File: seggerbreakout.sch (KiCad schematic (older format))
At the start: 3 parts, among them P1 SWD, P2 JTAG

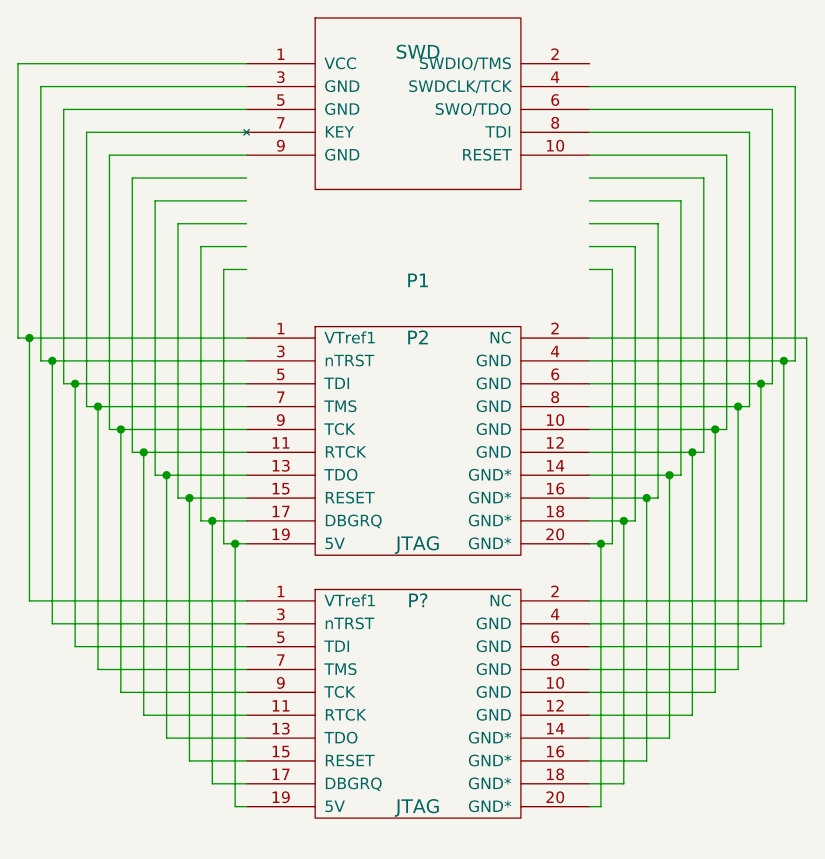
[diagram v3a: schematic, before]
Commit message: add swd and 2x5 swd connector
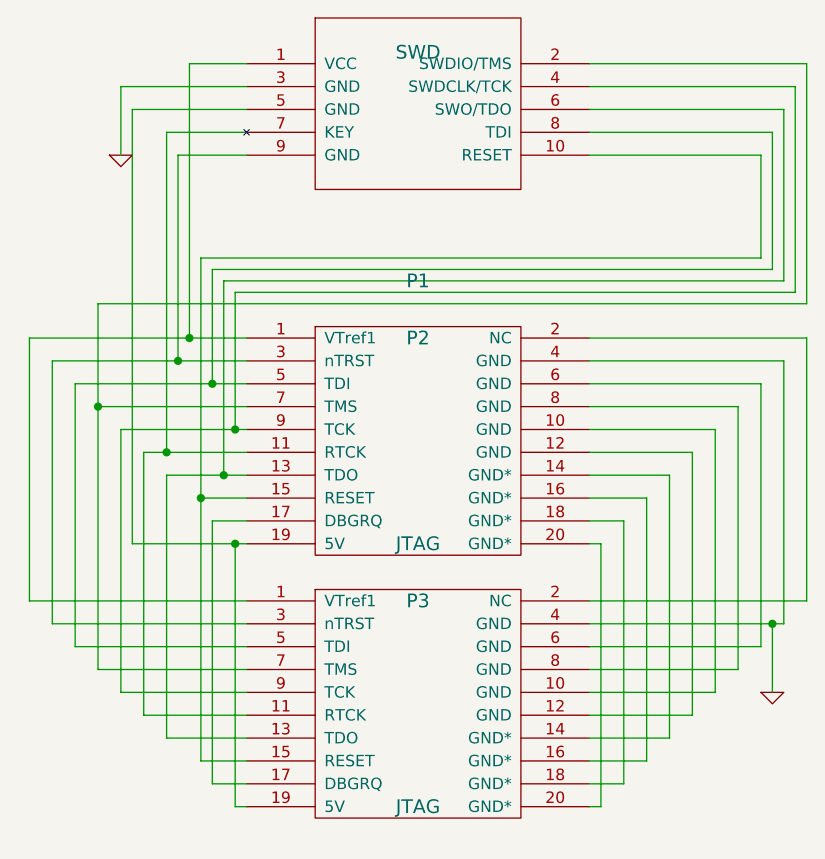
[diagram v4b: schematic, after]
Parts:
- gave numbers to parts that had none: 1
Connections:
- net labels added: GND
- wire segments 98 -> 89
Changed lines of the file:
@@
 Sheet 1 1
 Title ""
-Date "18 apr 2014"
+Date "18 aug 2014"
 Rev ""
 Comp ""
@@
 $EndComp
 $Comp
-L JTAG P?
+L JTAG P3
 U 1 1 53516C39
 P 5150 5700
-F 0 "P?" H 5150 6150 60  0000 C CNN
+F 0 "P3" H 5150 6150 60  0000 C CNN
 F 1 "JTAG" H 5150 5250 60  0000 C CNN
 F 2 "~" H 5050 5750 60  0000 C CNN
@@
 $EndComp
 Wire Wire Line
-	4300 5000 4400 5000
-Wire Wire Line
-	4300 5000 4300 3800
-Wire Wire Line
-	4300 3800 4400 3800
-Wire Wire Line
-	4400 3700 4200 3700
-Wire Wire Line
-	4200 3700 4200 4900
-Wire Wire Line
-	4200 4900 4400 4900
-Wire Wire Line
-	4400 3600 4100 3600
-Wire Wire Line
-	4100 3600 4100 4800
-Wire Wire Line
-	4100 4800 4400 4800
-Wire Wire Line
-	4400 3500 4000 3500
-Wire Wire Line
-	4000 3500 4000 4700
-Wire Wire Line
-	4000 4700 4400 4700
-Wire Wire Line
-	4400 3300 3800 3300
-Wire Wire Line
-	3800 3300 3800 4500
-Wire Wire Line
-	3800 4500 4400 4500
-Wire Wire Line
-	4400 3200 3700 3200
-Wire Wire Line
-	3700 3200 3700 4400
-Wire Wire Line
-	3700 4400 4400 4400
-Wire Wire Line
-	4400 3100 3600 3100
-Wire Wire Line
-	3600 3100 3600 4300
-Wire Wire Line
-	3600 4300 4400 4300
-Wire Wire Line
-	4400 3000 3500 3000
-Wire Wire Line
-	3500 3000 3500 4200
-Wire Wire Line
-	3500 4200 4400 4200
-Wire Wire Line
-	4400 2900 3400 2900
-Wire Wire Line
-	3400 2900 3400 4100
-Wire Wire Line
-	3400 4100 4400 4100
-Wire Wire Line
-	5900 3800 6000 3800
-Wire Wire Line
-	6000 3800 6000 5000
-Wire Wire Line
-	6000 5000 5900 5000
-Wire Wire Line
-	5900 4900 6100 4900
-Wire Wire Line
-	6100 4900 6100 3700
-Wire Wire Line
-	6100 3700 5900 3700
-Wire Wire Line
-	5900 4800 6200 4800
-Wire Wire Line
-	6200 4800 6200 3600
-Wire Wire Line
-	6200 3600 5900 3600
-Wire Wire Line
-	5900 4700 6300 4700
-Wire Wire Line
-	6300 4700 6300 3500
-Wire Wire Line
-	6300 3500 5900 3500
-Wire Wire Line
-	5900 4600 6400 4600
-Wire Wire Line
-	6400 4600 6400 3400
-Wire Wire Line
-	6400 3400 5900 3400
-Wire Wire Line
-	5900 4500 6500 4500
-Wire Wire Line
-	6500 4500 6500 3300
-Wire Wire Line
-	6500 3300 5900 3300
-Wire Wire Line
-	5900 4400 6600 4400
-Wire Wire Line
-	6600 4400 6600 3200
-Wire Wire Line
-	6600 3200 5900 3200
-Wire Wire Line
-	5900 4300 6700 4300
-Wire Wire Line
-	6700 4300 6700 3100
-Wire Wire Line
-	6700 3100 5900 3100
-Wire Wire Line
-	5900 4200 6800 4200
-Wire Wire Line
-	6800 4200 6800 3000
+	4350 5000 4350 6150
+Wire Wire Line
+	4350 6150 4400 6150
+Wire Wire Line
+	4250 4900 4250 6050
+Wire Wire Line
+	4250 6050 4400 6050
+Wire Wire Line
+	4050 4700 4050 5850
+Wire Wire Line
+	4050 5850 4400 5850
+Wire Wire Line
+	3950 4600 3950 5750
+Wire Wire Line
+	3950 5750 4400 5750
+Wire Wire Line
+	3850 4500 3850 5650
+Wire Wire Line
+	3850 5650 4400 5650
+Wire Wire Line
+	3750 3950 3750 5550
+Wire Wire Line
+	3750 5550 4400 5550
+Wire Wire Line
+	3650 4300 3650 5450
+Wire Wire Line
+	3650 5450 4400 5450
+Wire Wire Line
+	3550 4200 3550 5350
+Wire Wire Line
+	3550 5350 4400 5350
+Wire Wire Line
+	5950 5000 5950 6150
+Wire Wire Line
+	5950 6150 5900 6150
+Wire Wire Line
+	6050 4900 6050 6050
+Wire Wire Line
+	6050 6050 5900 6050
+Wire Wire Line
+	6150 4800 6150 5950
+Wire Wire Line
+	6150 5950 5900 5950
+Wire Wire Line
+	6250 4700 6250 5850
+Wire Wire Line
+	6250 5850 5900 5850
+Wire Wire Line
+	6350 4600 6350 5750
+Wire Wire Line
+	6350 5750 5900 5750
+Wire Wire Line
+	6450 4500 6450 5650
+Wire Wire Line
+	6450 5650 5900 5650
+Wire Wire Line
+	6550 4400 6550 5550
+Wire Wire Line
+	6550 5550 5900 5550
+Wire Wire Line
+	6650 4300 6650 5450
+Wire Wire Line
+	6650 5450 5900 5450
+Wire Wire Line
+	6750 4200 6750 5350
+Wire Wire Line
+	6750 5350 5900 5350
+Wire Wire Line
+	5900 4100 6850 4100
+Wire Wire Line
+	6850 4100 6850 5250
+Wire Wire Line
+	6850 5250 5900 5250
+Wire Wire Line
+	3450 4100 3450 5250
+Wire Wire Line
+	3450 5250 4400 5250
+Wire Wire Line
+	3750 4400 4400 4400
+Wire Wire Line
+	3750 3950 6850 3950
+Wire Wire Line
+	6850 3950 6850 2900
+Connection ~ 3750 4400
+Wire Wire Line
+	3650 4300 4400 4300
+Wire Wire Line
+	4400 4200 3550 4200
+Wire Wire Line
+	6750 4200 5900 4200
+Wire Wire Line
+	4400 4100 3450 4100
+Wire Wire Line
+	6850 2900 5900 2900
+Wire Wire Line
+	3850 4500 4400 4500
+Wire Wire Line
+	4350 4500 4350 3900
+Wire Wire Line
+	4350 3900 6800 3900
+Wire Wire Line
+	6800 3900 6800 3000
 Wire Wire Line
 	6800 3000 5900 3000
 Wire Wire Line
-	4400 3400 3900 3400
-Wire Wire Line
-	3900 3400 3900 4600
-Wire Wire Line
-	3900 4600 4400 4600
-Wire Wire Line
-	4350 5000 4350 6150
-Wire Wire Line
-	4350 6150 4400 6150
+	4050 4700 4400 4700
+Wire Wire Line
+	4300 4700 4300 3850
+Wire Wire Line
+	4300 3850 6750 3850
+Wire Wire Line
+	6750 3850 6750 3100
+Wire Wire Line
+	6750 3100 5900 3100
+Wire Wire Line
+	4250 4300 4250 3800
+Wire Wire Line
+	4250 3800 6700 3800
+Wire Wire Line
+	6700 3800 6700 3200
+Wire Wire Line
+	6700 3200 5900 3200
+Connection ~ 4250 4300
+Wire Wire Line
+	4400 4800 4200 4800
+Wire Wire Line
+	4200 3750 4200 5950
+Wire Wire Line
+	4200 3750 6650 3750
+Wire Wire Line
+	6650 3750 6650 3300
+Wire Wire Line
+	6650 3300 5900 3300
+Wire Wire Line
+	4400 2900 4150 2900
+Wire Wire Line
+	4150 2900 4150 4100
+Connection ~ 4150 4100
+Wire Wire Line
+	3900 5000 4400 5000
+Wire Wire Line
+	4250 4900 4400 4900
+Wire Wire Line
+	4200 5950 4400 5950
+Connection ~ 4200 4800
+Connection ~ 4300 4700
+Wire Wire Line
+	3950 4600 4400 4600
+Connection ~ 4350 4500
+Wire Wire Line
+	4400 3300 4100 3300
+Wire Wire Line
+	4100 3300 4100 4200
+Connection ~ 4100 4200
+Wire Wire Line
+	4400 3200 4050 3200
+Wire Wire Line
+	4050 3200 4050 4600
+Connection ~ 4050 4600
+Wire Wire Line
+	4400 3000 3850 3000
+Wire Wire Line
+	3850 3000 3850 3300
+$Comp
+L GND #PWR?
+U 1 1 53F244EF
+P 3850 3300
+F 0 "#PWR?" H 3850 3300 30  0001 C CNN
+F 1 "GND" H 3850 3230 30  0001 C CNN
+F 2 "" H 3850 3300 60  0000 C CNN
+F 3 "" H 3850 3300 60  0000 C CNN
+	1    3850 3300
+	1    0    0    -1
+$EndComp
+$Comp
+L GND #PWR?
+U 1 1 53F244FC
+P 6700 5650
+F 0 "#PWR?" H 6700 5650 30  0001 C CNN
+F 1 "GND" H 6700 5580 30  0001 C CNN
+F 2 "" H 6700 5650 60  0000 C CNN
+F 3 "" H 6700 5650 60  0000 C CNN
+	1    6700 5650
+	1    0    0    -1
+$EndComp
+Wire Wire Line
+	6700 5350 6700 5650
+Connection ~ 6700 5350
+Wire Wire Line
+	4400 3100 3900 3100
+Wire Wire Line
+	3900 3100 3900 5000
 Connection ~ 4350 5000
 Wire Wire Line
-	4250 4900 4250 6050
-Wire Wire Line
-	4250 6050 4400 6050
-Connection ~ 4250 4900
-Wire Wire Line
-	4150 4800 4150 5950
-Wire Wire Line
-	4150 5950 4400 5950
-Connection ~ 4150 4800
-Wire Wire Line
-	4050 4700 4050 5850
-Wire Wire Line
-	4050 5850 4400 5850
-Connection ~ 4050 4700
-Wire Wire Line
-	3950 4600 3950 5750
-Wire Wire Line
-	3950 5750 4400 5750
-Connection ~ 3950 4600
-Wire Wire Line
-	3850 4500 3850 5650
-Wire Wire Line
-	3850 5650 4400 5650
-Connection ~ 3850 4500
-Wire Wire Line
-	3750 4400 3750 5550
-Wire Wire Line
-	3750 5550 4400 5550
-Connection ~ 3750 4400
-Wire Wire Line
-	3650 4300 3650 5450
-Wire Wire Line
-	3650 5450 4400 5450
-Connection ~ 3650 4300
-Wire Wire Line
-	3550 4200 3550 5350
-Wire Wire Line
-	3550 5350 4400 5350
-Connection ~ 3550 4200
-Wire Wire Line
-	5950 5000 5950 6150
-Wire Wire Line
-	5950 6150 5900 6150
-Connection ~ 5950 5000
-Wire Wire Line
-	6050 4900 6050 6050
-Wire Wire Line
-	6050 6050 5900 6050
-Connection ~ 6050 4900
-Wire Wire Line
-	6150 4800 6150 5950
-Wire Wire Line
-	6150 5950 5900 5950
-Connection ~ 6150 4800
-Wire Wire Line
-	6250 4700 6250 5850
-Wire Wire Line
-	6250 5850 5900 5850
-Connection ~ 6250 4700
-Wire Wire Line
-	6350 4600 6350 5750
-Wire Wire Line
-	6350 5750 5900 5750
-Connection ~ 6350 4600
-Wire Wire Line
-	6450 4500 6450 5650
-Wire Wire Line
-	6450 5650 5900 5650
-Connection ~ 6450 4500
-Wire Wire Line
-	6550 4400 6550 5550
-Wire Wire Line
-	6550 5550 5900 5550
-Connection ~ 6550 4400
-Wire Wire Line
-	6650 4300 6650 5450
-Wire Wire Line
-	6650 5450 5900 5450
-Connection ~ 6650 4300
-Wire Wire Line
-	6750 4200 6750 5350
-Wire Wire Line
-	6750 5350 5900 5350
-Connection ~ 6750 4200
-Wire Wire Line
-	5900 4100 6850 4100
-Wire Wire Line
-	6850 4100 6850 5250
-Wire Wire Line
-	6850 5250 5900 5250
-Wire Wire Line
-	3450 4100 3450 5250
-Wire Wire Line
-	3450 5250 4400 5250
-Connection ~ 3450 4100
+	5950 5000 5900 5000
+Wire Wire Line
+	5900 4900 6050 4900
+Wire Wire Line
+	6150 4800 5900 4800
+Wire Wire Line
+	5900 4700 6250 4700
+Wire Wire Line
+	6350 4600 5900 4600
+Wire Wire Line
+	5900 4500 6450 4500
+Wire Wire Line
+	6550 4400 5900 4400
+Wire Wire Line
+	5900 4300 6650 4300
 $EndSCHEMATC

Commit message: Add cleaner bus routed version
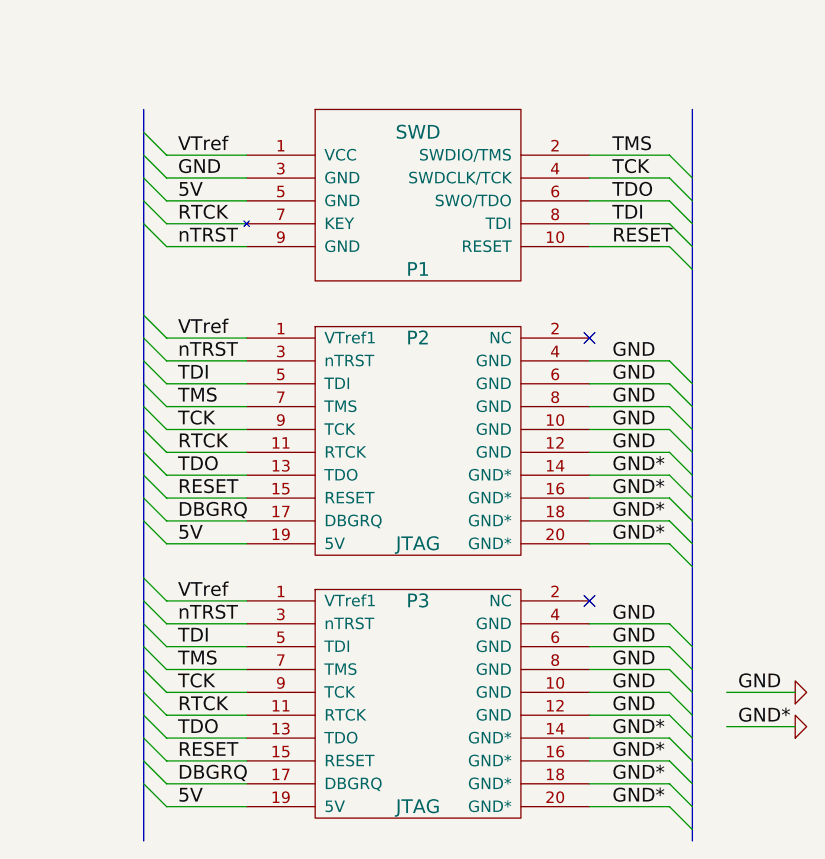
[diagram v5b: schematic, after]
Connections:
- net GND: now also P2.10 (GND), P2.12 (GND), P2.14 (GND*), P2.16 (GND*), P2.18 (GND*), P2.20 (GND*), P2.6 (GND), P2.8 (GND), P3.10 (GND), P3.12 (GND), P3.14 (GND*), P3.16 (GND*), P3.18 (GND*), P3.20 (GND*), P3.6 (GND), P3.8 (GND)
- net VTref: now reaches P1.1 (VCC), P2.1 (VTref1), P3.1 (VTref1)
- net RTCK: now reaches P1.7 (KEY), P2.11 (RTCK), P3.11 (RTCK)
- net TDO: now reaches P1.6 (SWO/TDO), P2.13 (TDO), P3.13 (TDO)
- net RESET: now reaches P1.10 (RESET), P2.15 (RESET), P3.15 (RESET)
- net DBGRQ: now reaches P2.17 (DBGRQ), P3.17 (DBGRQ)
- net 5V: now reaches P1.5 (GND), P2.19 (5V), P3.19 (5V)
- net at P2.2 (NC): no longer P3.2 (NC)
- net nTRST: now reaches P1.9 (GND), P2.3 (nTRST), P3.3 (nTRST)
- net TDI: now reaches P1.8 (TDI), P2.5 (TDI), P3.5 (TDI)
- net TMS: now reaches P1.2 (SWDIO/TMS), P2.7 (TMS), P3.7 (TMS)
- net TCK: now reaches P1.4 (SWDCLK/TCK), P2.9 (TCK), P3.9 (TCK)
- no-connect marks 0 -> 2

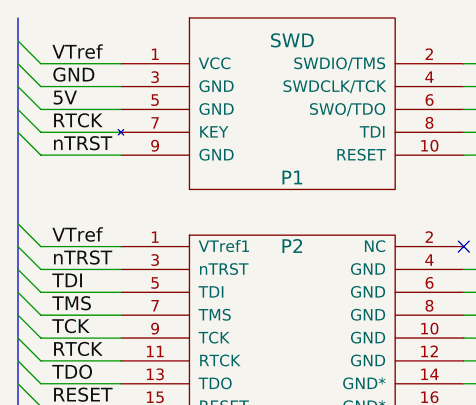
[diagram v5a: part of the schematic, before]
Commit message: Correct SWD pinout on schematic and footprint
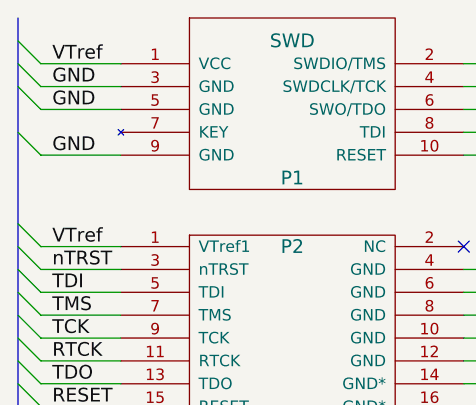
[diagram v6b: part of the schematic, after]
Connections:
- wire segments 50 -> 49
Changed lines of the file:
@@
 Sheet 1 1
 Title ""
-Date "18 aug 2014"
+Date "2 oct 2014"
 Rev ""
 Comp ""
@@
 	3950 3400 4050 3500
 Entry Wire Line
-	3950 3500 4050 3600
-Entry Wire Line
 	3950 3600 4050 3700
 Wire Wire Line
@@
 Wire Wire Line
 	4400 3500 4050 3500
-Wire Wire Line
-	4400 3600 4050 3600
 Wire Wire Line
 	4400 3700 4050 3700
@@
 	3950 3100 3950 6300
 Text Label 4100 3500 0    60   ~ 0
-5V
+GND
 Text Label 4100 5000 0    60   ~ 0
 5V
@@
 Text Label 4100 3400 0    60   ~ 0
 GND
-Text Label 4100 3600 0    60   ~ 0
-RTCK
 Text Label 4100 4600 0    60   ~ 0
 RTCK
@@
 TCK
 Text Label 4100 3700 0    60   ~ 0
-nTRST
+GND
 Text Label 4100 4400 0    60   ~ 0
 TMS
